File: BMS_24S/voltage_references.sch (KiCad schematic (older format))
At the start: 50 parts, among them Q201 BC558, U201 TL431LP, U202 LM324, U203 TL431LP, U204 TL431LP

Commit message: update balancing circuit
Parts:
- C202, C203, C205, C207, C209, C210: LCSC (none) -> C49678; Precision (none) -> 10%; Voltage (none) -> 50V
- R203, R204, R205, R207, R208, R209, R212, R213, R214, R215, R216, R217, R222, R223, R225, R228: LCSC (none) -> C17513; Power (none) -> 1/8W; Precision (none) -> 1%; Voltage (none) -> 150V
- R206, R220: LCSC (none) -> C17414; Power (none) -> 1/8W; Precision (none) -> 1%; Voltage (none) -> 150V

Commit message: updates made on BMS
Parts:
- renumbered C203 to C201, C204 to C202, C208 to C203, C209 to C204, C201 to C205, C202 to C206, C205 to C207, C206 to C208, C210 to C209, C211 to C210, C207 to C211, R225 to R202, R211 to R203, R213 to R204, R226 to R205, R215 to R206, R221 to R207, R223 to R208, R229 to R209, R202 to R210, R227 to R211, R208 to R212, R218 to R213, R228 to R215, R203 to R216, R205 to R217, R207 to R218, R209 to R219, R224 to R220, R212 to R221, R219 to R222, R230 to R223, R220 to R224, R222 to R225, R216 to R226, R210 to R227, R217 to R228, R204 to R229, R206 to R230, TP202 to TP201, TP203 to TP202, TP204 to TP203, TP201 to TP204, U202 to U201, U203 to U202, U201 to U203

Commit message: get BSPD
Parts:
- R201, R210: LCSC (none) -> C17408
- R203, R209, R213, R220, R222, R223, R227: LCSC (none) -> C17477
- U201: LCSC (none) -> C71035
- U202, U203, U204: LCSC (none) -> C181103
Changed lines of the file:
@@
 F 2 "Resistor_SMD:R_0805_2012Metric" V 930 950 50  0001 C CNN
 F 3 "~" H 1000 950 50  0001 C CNN
+F 4 "C17408" H 1000 950 50  0001 C CNN "LCSC"
 	1    1000 950
 	1    0    0    -1
@@
 F 2 "Package_SO:SOIC-14_3.9x8.7mm_P1.27mm" H 2300 1725 50  0001 C CNN
 F 3 "http://www.ti.com/lit/ds/symlink/lm2902-n.pdf" H 2350 2200 50  0001 C CNN
+F 4 "C71035" H 2300 2000 50  0001 C CNN "LCSC"
 	1    2300 2000
 	1    0    0    -1
@@
 F 2 "Package_SO:SOIC-14_3.9x8.7mm_P1.27mm" H 2300 725 50  0001 C CNN
 F 3 "http://www.ti.com/lit/ds/symlink/lm2902-n.pdf" H 2350 1200 50  0001 C CNN
+F 4 "C71035" H 2300 1000 50  0001 C CNN "LCSC"
 	2    2300 1000
 	1    0    0    -1
@@
 F 2 "Package_SO:SOIC-14_3.9x8.7mm_P1.27mm" H 5100 1675 50  0001 C CNN
 F 3 "http://www.ti.com/lit/ds/symlink/lm2902-n.pdf" H 5150 2150 50  0001 C CNN
+F 4 "C71035" H 5100 1950 50  0001 C CNN "LCSC"
 	3    5100 1950
 	1    0    0    -1
@@
 F 2 "Resistor_SMD:R_0805_2012Metric" V 930 1300 50  0001 C CNN
 F 3 "~" H 1000 1300 50  0001 C CNN
+F 4 "C17408" H 1000 1300 50  0001 C CNN "LCSC"
 	1    1000 1300
 	1    0    0    -1
@@
 F 2 "Package_TO_SOT_SMD:SOT-23" H 1000 1500 50  0001 C CIN
 F 3 "http://www.ti.com/lit/ds/symlink/tl431.pdf" H 1000 1650 50  0001 C CIN
+F 4 "C181103" H 1000 1650 50  0001 C CNN "LCSC"
 	1    1000 1650
 	0    1    -1   0
@@
 F 2 "Package_TO_SOT_SMD:SOT-23" H 3400 1100 50  0001 C CIN
 F 3 "http://www.ti.com/lit/ds/symlink/tl431.pdf" H 3400 1250 50  0001 C CIN
+F 4 "C181103" H 3400 1250 50  0001 C CNN "LCSC"
 	1    3400 1250
 	0    1    -1   0
@@
 F 2 "Package_TO_SOT_SMD:SOT-23" H 4100 2000 50  0001 C CIN
 F 3 "http://www.ti.com/lit/ds/symlink/tl431.pdf" H 4100 2150 50  0001 C CIN
+F 4 "C181103" H 4100 2150 50  0001 C CNN "LCSC"
 	1    4100 2150
 	0    1    -1   0
@@
 F 2 "Resistor_SMD:R_0805_2012Metric" V 6680 1200 50  0001 C CNN
 F 3 "~" H 6750 1200 50  0001 C CNN
+F 4 "C17477" H 6750 1200 50  0001 C CNN "LCSC"
 	1    6750 1200
 	-1   0    0    1
@@
 F 2 "Resistor_SMD:R_0805_2012Metric" V 6180 1650 50  0001 C CNN
 F 3 "~" H 6250 1650 50  0001 C CNN
+F 4 "C17477" H 6250 1650 50  0001 C CNN "LCSC"
 	1    6250 1650
 	1    0    0    -1
@@
 F 2 "Package_SO:SOIC-14_3.9x8.7mm_P1.27mm" H 2250 2925 50  0001 C CNN
 F 3 "http://www.ti.com/lit/ds/symlink/lm2902-n.pdf" H 2300 3400 50  0001 C CNN
+F 4 "C71035" H 2250 3200 50  0001 C CNN "LCSC"
 	5    2250 3200
 	0    1    1    0
@@
 F 2 "Resistor_SMD:R_0805_2012Metric" V 2780 1000 50  0001 C CNN
 F 3 "~" H 2850 1000 50  0001 C CNN
+F 4 "C17477" H 2850 1000 50  0001 C CNN "LCSC"
 	1    2850 1000
 	0    1    1    0
@@
 F 2 "Resistor_SMD:R_0805_2012Metric" V 5380 1800 50  0001 C CNN
 F 3 "~" H 5450 1800 50  0001 C CNN
+F 4 "C17477" H 5450 1800 50  0001 C CNN "LCSC"
 	1    5450 1800
 	-1   0    0    1
@@
 F 2 "Resistor_SMD:R_0805_2012Metric" V 7080 1800 50  0001 C CNN
 F 3 "~" H 7150 1800 50  0001 C CNN
+F 4 "C17477" H 7150 1800 50  0001 C CNN "LCSC"
 	1    7150 1800
 	-1   0    0    1
@@
 F 2 "Resistor_SMD:R_0805_2012Metric" V 2680 2200 50  0001 C CNN
 F 3 "~" H 2750 2200 50  0001 C CNN
+F 4 "C17477" H 2750 2200 50  0001 C CNN "LCSC"
 	1    2750 2200
 	1    0    0    -1
@@
 F 2 "Resistor_SMD:R_0805_2012Metric" V 5380 1400 50  0001 C CNN
 F 3 "~" H 5450 1400 50  0001 C CNN
+F 4 "C17477" H 5450 1400 50  0001 C CNN "LCSC"
 	1    5450 1400
 	-1   0    0    1
@@
 F 2 "Package_SO:SOIC-14_3.9x8.7mm_P1.27mm" H 6800 1775 50  0001 C CNN
 F 3 "http://www.ti.com/lit/ds/symlink/lm2902-n.pdf" H 6850 2250 50  0001 C CNN
+F 4 "C71035" H 6800 2050 50  0001 C CNN "LCSC"
 	4    6800 2050
 	1    0    0    -1

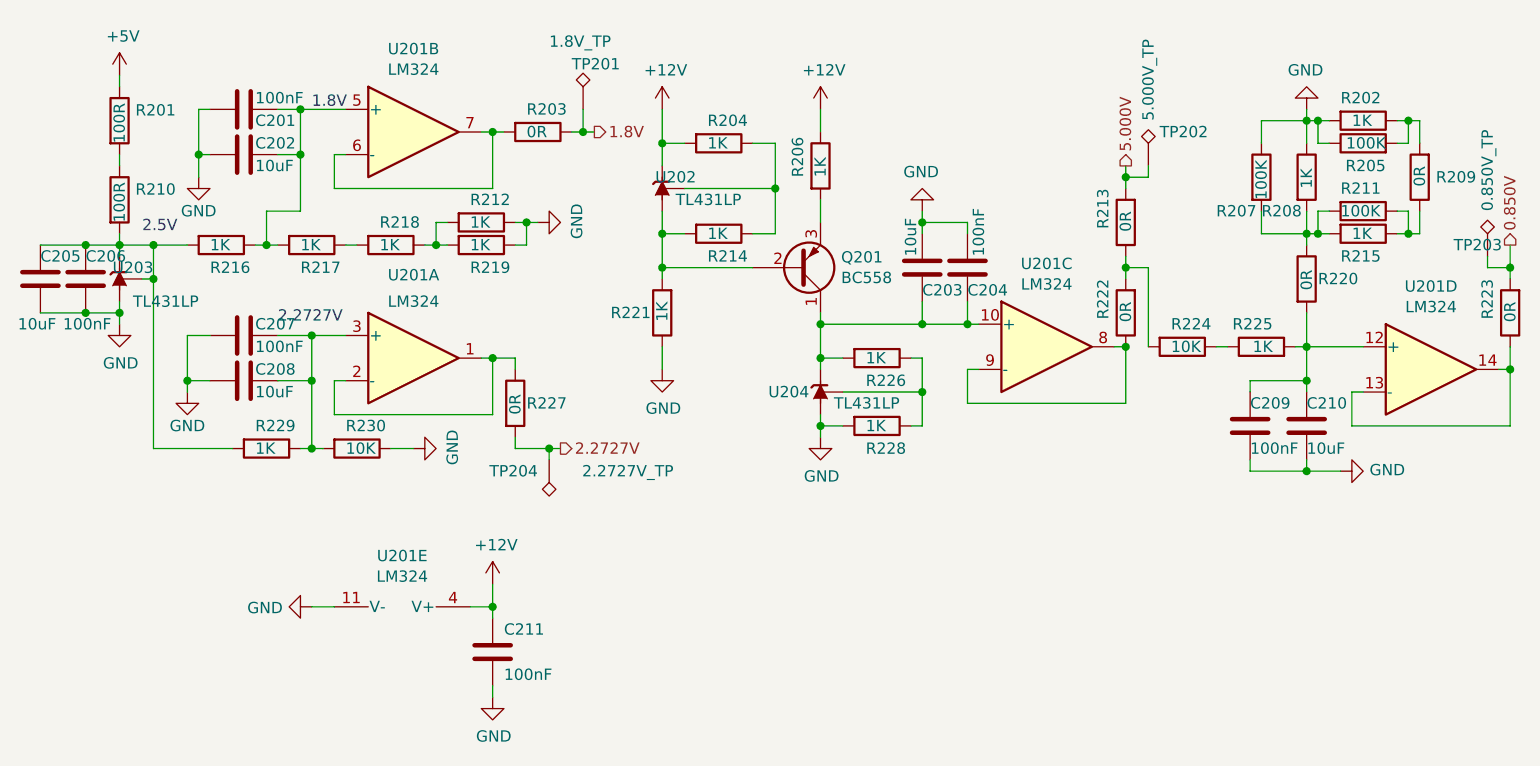
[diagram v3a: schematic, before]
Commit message: update bms pcb
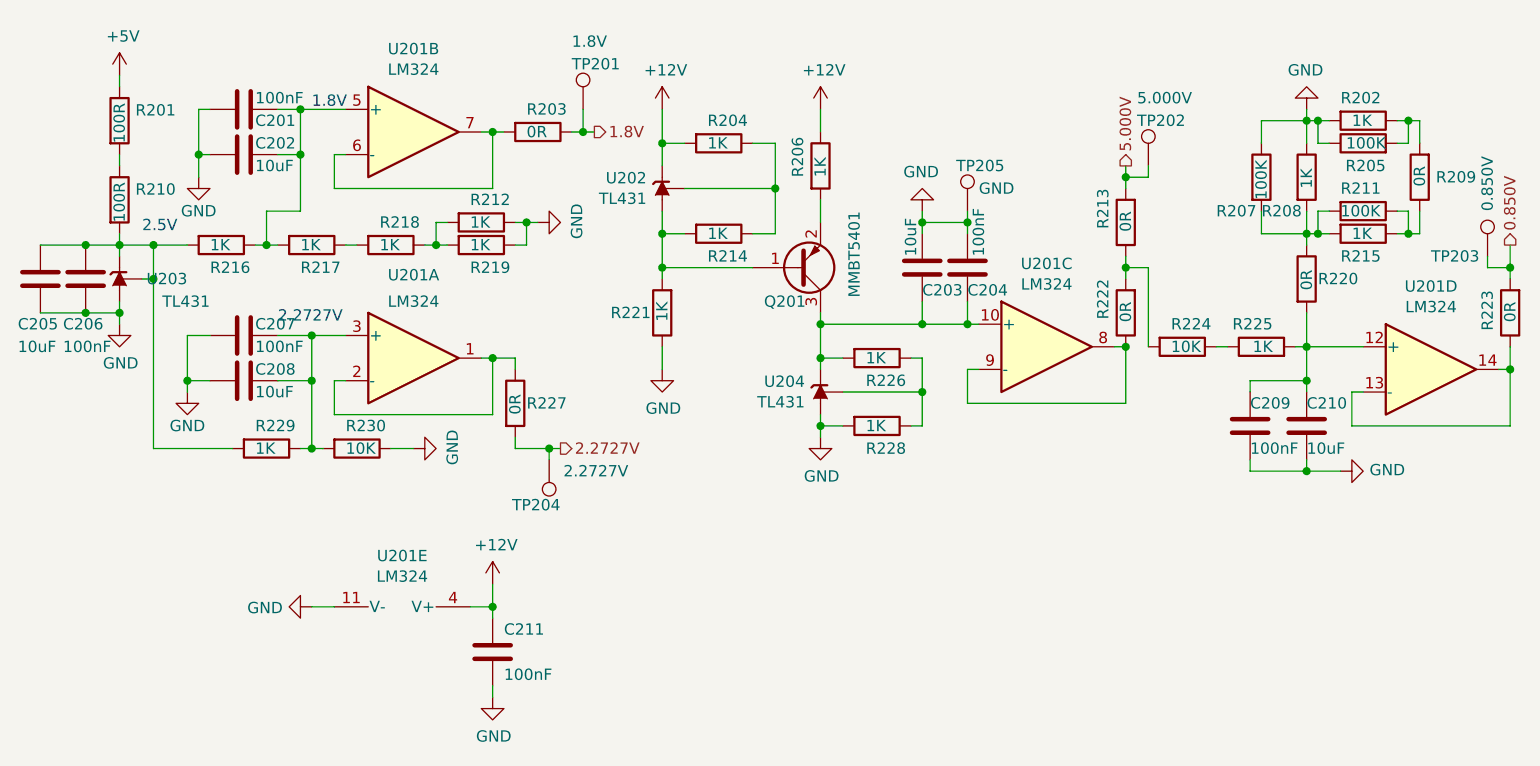
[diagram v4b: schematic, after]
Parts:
- removed Q201: BC558, Package_TO_SOT_SMD:SOT-23, symbol Transistor_BJT:BC558
- removed TP201: 1.8V_TP, TestPoint:TestPoint_Pad_2.5x2.5mm, symbol Connector:TestPoint_Alt
- removed TP202: 5.000V_TP, TestPoint:TestPoint_Pad_2.5x2.5mm, symbol Connector:TestPoint_Alt
- removed TP203: 0.850V_TP, TestPoint:TestPoint_Pad_2.5x2.5mm, symbol Connector:TestPoint_Alt
- removed TP204: 2.2727V_TP, TestPoint:TestPoint_Pad_2.5x2.5mm, symbol Connector:TestPoint_Alt
- removed U202, U203, U204: TL431LP, Package_TO_SOT_SMD:SOT-23, symbol e-Power:TL431LP
- added Q201: MMBT5401, Package_TO_SOT_SMD:SOT-23, symbol Transistor_BJT:MMBTA92
- added TP201: 1.8V, e-Power:TestPoint_Pad_D1.0mm, symbol Connector:TestPoint
- added TP202: 5.000V, e-Power:TestPoint_Pad_D1.0mm, symbol Connector:TestPoint
- added TP203: 0.850V, e-Power:TestPoint_Pad_D1.0mm, symbol Connector:TestPoint
- added TP204: 2.2727V, e-Power:TestPoint_Pad_D1.0mm, symbol Connector:TestPoint
- added TP205: GND, e-Power:TestPoint_Pad_D1.0mm, symbol Connector:TestPoint
- added U202, U204: TL431, Package_TO_SOT_SMD:SOT-23, symbol e-Power:TL431
- added U203: TL431, Package_TO_SOT_SMD:SOT-23, symbol Reference_Voltage:TL432DBZ
- C202, C203, C205, C208, C210: LCSC (none) -> C15850
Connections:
- net +12V: now also U202.2 (K)
- net 0.850V: now also TP203.1
- net 1.8V: now also TP201.1
- net 2.2727V: now also TP204.1
- net 5.000V: now also TP202.1
- net GND: now also TP205.1, U203.3 (A), U204.3 (A)
- net at C203.2, C204.2, R226.2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: now also Q201.3 (C), U204.2 (K)
- net at C205.1, C206.1, R210.2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: now also U203.1 (REF), U203.2 (K)
- net at R204.1, R214.1: now also U202.1 (REF)
- net at R214.2, R221.2: now also Q201.1 (B), U202.3 (A)
- net at R206.2: now also Q201.2 (E)
- net at R226.1, R228.1: now also U204.1 (REF)
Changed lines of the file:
@@
-$EndComp
-$Comp
-L e-Power:TL431LP U203
-U 1 1 5EB8B33D
-P 1000 1650
-F 0 "U203" V 1050 1800 50  0000 R CNN
-F 1 "TL431LP" V 900 2000 50  0000 R CNN
-F 2 "Package_TO_SOT_SMD:SOT-23" H 1000 1500 50  0001 C CIN
-F 3 "http://www.ti.com/lit/ds/symlink/tl431.pdf" H 1000 1650 50  0001 C CIN
-F 4 "C181103" H 1000 1650 50  0001 C CNN "LCSC"
-	1    1000 1650
-	0    1    -1   0
 $EndComp
 $Comp
@@
 U 1 1 5EB8E025
 P 850 1650
-F 0 "C206" H 850 1750 50  0000 L CNN
-F 1 "100nF" H 750 1450 50  0000 L CNN
+F 0 "C206" H 750 1450 50  0000 L CNN
+F 1 "100nF" H 750 1350 50  0000 L CNN
 F 2 "Capacitor_SMD:C_0805_2012Metric" H 888 1500 50  0001 C CNN
 F 3 "https://datasheet.lcsc.com/szlcsc/YAGEO-CC0805KRX7R9BB104_C49678.pdf" H 850 1650 50  0001 C CNN
@@
 U 1 1 5EB8ED80
 P 650 1650
-F 0 "C205" H 650 1750 50  0000 L CNN
-F 1 "10uF" H 550 1450 50  0000 L CNN
+F 0 "C205" H 550 1450 50  0000 L CNN
+F 1 "10uF" H 550 1350 50  0000 L CNN
 F 2 "Capacitor_SMD:C_0805_2012Metric" H 688 1500 50  0001 C CNN
 F 3 "~" H 650 1650 50  0001 C CNN
+F 4 "C15850" H 650 1650 50  0001 C CNN "LCSC"
 	1    650  1650
 	1    0    0    -1
@@
 F 2 "Capacitor_SMD:C_0805_2012Metric" H 1588 1950 50  0001 C CNN
 F 3 "~" H 1550 2100 50  0001 C CNN
+F 4 "C15850" H 1550 2100 50  0001 C CNN "LCSC"
 	1    1550 2100
 	0    1    1    0
@@
 F 2 "Capacitor_SMD:C_0805_2012Metric" H 1588 950 50  0001 C CNN
 F 3 "~" H 1550 1100 50  0001 C CNN
+F 4 "C15850" H 1550 1100 50  0001 C CNN "LCSC"
 	1    1550 1100
 	0    1    1    0
@@
 Wire Wire Line
 	2400 1500 2450 1500
-$Comp
-L e-Power:TL431LP U202
-U 1 1 5EBF269C
-P 3400 1250
-F 0 "U202" V 3450 1400 50  0000 R CNN
-F 1 "TL431LP" V 3350 1600 50  0000 R CNN
-F 2 "Package_TO_SOT_SMD:SOT-23" H 3400 1100 50  0001 C CIN
-F 3 "http://www.ti.com/lit/ds/symlink/tl431.pdf" H 3400 1250 50  0001 C CIN
-F 4 "C181103" H 3400 1250 50  0001 C CNN "LCSC"
-	1    3400 1250
-	0    1    -1   0
-$EndComp
 $Comp
 L power:+12V #PWR0202
@@
 	3400 1450 3400 1600
 $Comp
-L Transistor_BJT:BC558 Q201
-U 1 1 5EC10A29
-P 4000 1600
-F 0 "Q201" H 4191 1554 50  0000 L CNN
-F 1 "BC558" H 4191 1645 50  0000 L CNN
-F 2 "Package_TO_SOT_SMD:SOT-23" H 4200 1525 50  0001 L CIN
-F 3 "http://www.fairchildsemi.com/ds/BC/BC557.pdf" H 4000 1600 50  0001 L CNN
-	1    4000 1600
-	1    0    0    1
-$EndComp
-$Comp
 L Device:R R206
 U 1 1 5EC13E72
@@
 	3400 1600 3400 1650
 $Comp
-L e-Power:TL431LP U204
-U 1 1 5EC1FBC6
-P 4100 2150
-F 0 "U204" V 4100 2100 50  0000 R CNN
-F 1 "TL431LP" V 4050 2500 50  0000 R CNN
-F 2 "Package_TO_SOT_SMD:SOT-23" H 4100 2000 50  0001 C CIN
-F 3 "http://www.ti.com/lit/ds/symlink/tl431.pdf" H 4100 2150 50  0001 C CIN
-F 4 "C181103" H 4100 2150 50  0001 C CNN "LCSC"
-	1    4100 2150
-	0    1    -1   0
-$EndComp
-$Comp
 L power:GND #PWR0211
 U 1 1 5EC2095C
@@
 F 2 "Capacitor_SMD:C_0805_2012Metric" H 4588 1450 50  0001 C CNN
 F 3 "~" H 4550 1600 50  0001 C CNN
+F 4 "C15850" H 4550 1600 50  0001 C CNN "LCSC"
 	1    4550 1600
 	1    0    0    -1
@@
 F 2 "Capacitor_SMD:C_0805_2012Metric" H 6288 2150 50  0001 C CNN
 F 3 "~" H 6250 2300 50  0001 C CNN
+F 4 "C15850" H 6250 2300 50  0001 C CNN "LCSC"
 	1    6250 2300
 	1    0    0    -1
@@
 U 1 1 5EBB9479
 P 7150 1800
-F 0 "R223" V 7250 1650 50  0000 L CNN
+F 0 "R223" V 7250 1700 50  0000 L CNN
 F 1 "0R" V 7150 1750 50  0000 L CNN
 F 2 "Resistor_SMD:R_0805_2012Metric" V 7080 1800 50  0001 C CNN
@@
 	1    0    0    -1
 $EndComp
-$Comp
-L Connector:TestPoint_Alt TP?
-U 1 1 5EE4B789
-P 3050 900
-AR Path="/5ED9340F/5EE4B789" Ref="TP?"  Part="1"
-AR Path="/5EC1D7DE/5EE4B789" Ref="TP201"  Part="1"
-F 0 "TP201" H 3000 1100 50  0000 L CNN
-F 1 "1.8V_TP" H 2900 1200 50  0000 L CNN
-F 2 "TestPoint:TestPoint_Pad_2.5x2.5mm" H 3250 900 50  0001 C CNN
-F 3 "~" H 3250 900 50  0001 C CNN
-	1    3050 900
-	1    0    0    -1
-$EndComp
 Wire Wire Line
 	3050 900  3050 1000
@@
 Wire Wire Line
 	3050 1000 3000 1000
-$Comp
-L Connector:TestPoint_Alt TP?
-U 1 1 5EE5EAA4
+Wire Wire Line
+	2900 2450 2900 2400
+Connection ~ 2900 2400
+Wire Wire Line
+	2900 2400 2950 2400
+Wire Wire Line
+	5450 1150 5450 1200
+Wire Wire Line
+	5550 1150 5550 1200
+Wire Wire Line
+	5550 1200 5450 1200
+Connection ~ 5450 1200
+Wire Wire Line
+	5450 1200 5450 1250
+Wire Wire Line
+	7150 1500 7150 1600
+Wire Wire Line
+	7050 1550 7050 1600
+Wire Wire Line
+	7050 1600 7150 1600
+Connection ~ 7150 1600
+Wire Wire Line
+	7150 1600 7150 1650
+$Comp
+L Connector:TestPoint TP?
+U 1 1 5FB7FD92
 P 2900 2450
-AR Path="/5ED9340F/5EE5EAA4" Ref="TP?"  Part="1"
-AR Path="/5EC1D7DE/5EE5EAA4" Ref="TP204"  Part="1"
-F 0 "TP204" H 2950 2500 50  0000 L CNN
-F 1 "2.2727V_TP" H 2350 2500 50  0000 L CNN
-F 2 "TestPoint:TestPoint_Pad_2.5x2.5mm" H 3100 2450 50  0001 C CNN
+AR Path="/5ED9340F/5FB7FD92" Ref="TP?"  Part="1"
+AR Path="/5EC1D7DE/5FB7FD92" Ref="TP204"  Part="1"
+F 0 "TP204" H 2850 2650 50  0000 L CNN
+F 1 "2.2727V" H 2550 2500 50  0000 L CNN
+F 2 "e-Power:TestPoint_Pad_D1.0mm" H 3100 2450 50  0001 C CNN
 F 3 "~" H 3100 2450 50  0001 C CNN
 	1    2900 2450
 	-1   0    0    1
 $EndComp
-Wire Wire Line
-	2900 2450 2900 2400
-Connection ~ 2900 2400
-Wire Wire Line
-	2900 2400 2950 2400
-Wire Wire Line
-	5450 1150 5450 1200
-$Comp
-L Connector:TestPoint_Alt TP?
-U 1 1 5EE87F64
+$Comp
+L Connector:TestPoint TP?
+U 1 1 5FB877AE
+P 3050 900
+AR Path="/5ED9340F/5FB877AE" Ref="TP?"  Part="1"
+AR Path="/5EC1D7DE/5FB877AE" Ref="TP201"  Part="1"
+F 0 "TP201" H 3000 1100 50  0000 L CNN
+F 1 "1.8V" H 3000 1200 50  0000 L CNN
+F 2 "e-Power:TestPoint_Pad_D1.0mm" H 3250 900 50  0001 C CNN
+F 3 "~" H 3250 900 50  0001 C CNN
+	1    3050 900
+	1    0    0    -1
+$EndComp
+$Comp
+L Connector:TestPoint TP?
+U 1 1 5FB88B6A
 P 5550 1150
-AR Path="/5ED9340F/5EE87F64" Ref="TP?"  Part="1"
-AR Path="/5EC1D7DE/5EE87F64" Ref="TP202"  Part="1"
-F 0 "TP202" H 5600 1300 50  0000 L CNN
-F 1 "5.000V_TP" V 5550 1350 50  0000 L CNN
-F 2 "TestPoint:TestPoint_Pad_2.5x2.5mm" H 5750 1150 50  0001 C CNN
+AR Path="/5ED9340F/5FB88B6A" Ref="TP?"  Part="1"
+AR Path="/5EC1D7DE/5FB88B6A" Ref="TP202"  Part="1"
+F 0 "TP202" H 5500 1350 50  0000 L CNN
+F 1 "5.000V" H 5500 1450 50  0000 L CNN
+F 2 "e-Power:TestPoint_Pad_D1.0mm" H 5750 1150 50  0001 C CNN
 F 3 "~" H 5750 1150 50  0001 C CNN
 	1    5550 1150
 	1    0    0    -1
 $EndComp
-Wire Wire Line
-	5550 1150 5550 1200
-Wire Wire Line
-	5550 1200 5450 1200
-Connection ~ 5450 1200
-Wire Wire Line
-	5450 1200 5450 1250
-Wire Wire Line
-	7150 1500 7150 1600
-$Comp
-L Connector:TestPoint_Alt TP?
-U 1 1 5EEB48C9
+$Comp
+L Connector:TestPoint TP?
+U 1 1 5FB89627
 P 7050 1550
-AR Path="/5ED9340F/5EEB48C9" Ref="TP?"  Part="1"
-AR Path="/5EC1D7DE/5EEB48C9" Ref="TP203"  Part="1"
-F 0 "TP203" H 6900 1600 50  0000 L CNN
-F 1 "0.850V_TP" V 7050 1750 50  0000 L CNN
-F 2 "TestPoint:TestPoint_Pad_2.5x2.5mm" H 7250 1550 50  0001 C CNN
+AR Path="/5ED9340F/5FB89627" Ref="TP?"  Part="1"
+AR Path="/5EC1D7DE/5FB89627" Ref="TP203"  Part="1"
+F 0 "TP203" H 6800 1550 50  0000 L CNN
+F 1 "0.850V" V 7050 1750 50  0000 L CNN
+F 2 "e-Power:TestPoint_Pad_D1.0mm" H 7250 1550 50  0001 C CNN
 F 3 "~" H 7250 1550 50  0001 C CNN
 	1    7050 1550
 	1    0    0    -1
 $EndComp
-Wire Wire Line
-	7050 1550 7050 1600
-Wire Wire Line
-	7050 1600 7150 1600
-Connection ~ 7150 1600
-Wire Wire Line
-	7150 1600 7150 1650
+$Comp
+L Transistor_BJT:MMBTA92 Q201
+U 1 1 5FB8ADEC
+P 4000 1600
+F 0 "Q201" H 3850 1750 50  0000 L CNN
+F 1 "MMBT5401" V 4250 1350 50  0000 L CNN
+F 2 "Package_TO_SOT_SMD:SOT-23" H 4200 1525 50  0001 L CIN
+F 3 "https://datasheet.lcsc.com/szlcsc/Changjiang-Electronics-Tech-CJ-MMBT5401_C8326.pdf" H 4000 1600 50  0001 L CNN
+F 4 "C8326" H 4000 1600 50  0001 C CNN "LCSC"
+	1    4000 1600
+	1    0    0    1
+$EndComp
+$Comp
+L Reference_Voltage:TL432DBZ U203
+U 1 1 5FB99557
+P 1000 1650
+F 0 "U203" V 1000 1950 50  0000 R CNN
+F 1 "TL431" V 900 2050 50  0000 R CNN
+F 2 "Package_TO_SOT_SMD:SOT-23" H 1000 1500 50  0001 C CIN
+F 3 "http://www.ti.com/lit/ds/symlink/tl431.pdf" H 1000 1650 50  0001 C CIN
+	1    1000 1650
+	0    1    -1   0
+$EndComp
+$Comp
+L e-Power:TL431 U202
+U 1 1 5FBA715A
+P 3400 1250
+F 0 "U202" V 3446 1181 50  0000 R CNN
+F 1 "TL431" V 3355 1181 50  0000 R CNN
+F 2 "Package_TO_SOT_SMD:SOT-23" H 3400 1100 50  0001 C CIN
+F 3 "http://www.ti.com/lit/ds/symlink/tl431.pdf" H 3400 1250 50  0001 C CIN
+	1    3400 1250
+	0    1    -1   0
+$EndComp
+$Comp
+L e-Power:TL431 U204
+U 1 1 5FBA816C
+P 4100 2150
+F 0 "U204" V 4146 2081 50  0000 R CNN
+F 1 "TL431" V 4055 2081 50  0000 R CNN
+F 2 "Package_TO_SOT_SMD:SOT-23" H 4100 2000 50  0001 C CIN
+F 3 "http://www.ti.com/lit/ds/symlink/tl431.pdf" H 4100 2150 50  0001 C CIN
+	1    4100 2150
+	0    1    -1   0
+$EndComp
+$Comp
+L Connector:TestPoint TP?
+U 1 1 5FC6D345
+P 4750 1350
+AR Path="/5ED9340F/5FC6D345" Ref="TP?"  Part="1"
+AR Path="/5EC1D7DE/5FC6D345" Ref="TP205"  Part="1"
+F 0 "TP205" H 4700 1550 50  0000 L CNN
+F 1 "GND" H 4800 1450 50  0000 L CNN
+F 2 "e-Power:TestPoint_Pad_D1.0mm" H 4950 1350 50  0001 C CNN
+F 3 "~" H 4950 1350 50  0001 C CNN
+	1    4750 1350
+	1    0    0    -1
+$EndComp
+Wire Wire Line
+	4750 1350 4750 1400
+Connection ~ 4750 1400
 $EndSCHEMATC

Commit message: updates made on BMS
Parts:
- renumbered TP205 to TP203, TP203 to TP204, TP204 to TP205
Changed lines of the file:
@@
 P 2900 2450
 AR Path="/5ED9340F/5FB7FD92" Ref="TP?"  Part="1"
-AR Path="/5EC1D7DE/5FB7FD92" Ref="TP204"  Part="1"
-F 0 "TP204" H 2850 2650 50  0000 L CNN
+AR Path="/5EC1D7DE/5FB7FD92" Ref="TP205"  Part="1"
+F 0 "TP205" H 2850 2650 50  0000 L CNN
 F 1 "2.2727V" H 2550 2500 50  0000 L CNN
 F 2 "e-Power:TestPoint_Pad_D1.0mm" H 3100 2450 50  0001 C CNN
@@
 P 7050 1550
 AR Path="/5ED9340F/5FB89627" Ref="TP?"  Part="1"
-AR Path="/5EC1D7DE/5FB89627" Ref="TP203"  Part="1"
-F 0 "TP203" H 6800 1550 50  0000 L CNN
+AR Path="/5EC1D7DE/5FB89627" Ref="TP204"  Part="1"
+F 0 "TP204" H 6800 1550 50  0000 L CNN
 F 1 "0.850V" V 7050 1750 50  0000 L CNN
 F 2 "e-Power:TestPoint_Pad_D1.0mm" H 7250 1550 50  0001 C CNN
@@
 P 4750 1350
 AR Path="/5ED9340F/5FC6D345" Ref="TP?"  Part="1"
-AR Path="/5EC1D7DE/5FC6D345" Ref="TP205"  Part="1"
-F 0 "TP205" H 4700 1550 50  0000 L CNN
+AR Path="/5EC1D7DE/5FC6D345" Ref="TP203"  Part="1"
+F 0 "TP203" H 4700 1550 50  0000 L CNN
 F 1 "GND" H 4800 1450 50  0000 L CNN
 F 2 "e-Power:TestPoint_Pad_D1.0mm" H 4950 1350 50  0001 C CNN

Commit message: updates made on bms, almost done
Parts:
- R205, R207, R211: LCSC (none) -> C17407
- U202, U203, U204: LCSC (none) -> C3113
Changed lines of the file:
@@
 F 2 "Resistor_SMD:R_0805_2012Metric" V 6430 1350 50  0001 C CNN
 F 3 "~" H 6500 1350 50  0001 C CNN
+F 4 "C17407" H 6500 1350 50  0001 C CNN "LCSC"
 	1    6500 1350
 	0    1    1    0
@@
 F 2 "Resistor_SMD:R_0805_2012Metric" V 6430 1050 50  0001 C CNN
 F 3 "~" H 6500 1050 50  0001 C CNN
+F 4 "C17407" H 6500 1050 50  0001 C CNN "LCSC"
 	1    6500 1050
 	0    -1   -1   0
@@
 F 2 "Resistor_SMD:R_0805_2012Metric" V 5980 1200 50  0001 C CNN
 F 3 "~" H 6050 1200 50  0001 C CNN
+F 4 "C17407" H 6050 1200 50  0001 C CNN "LCSC"
 	1    6050 1200
 	1    0    0    -1
@@
 F 2 "Package_TO_SOT_SMD:SOT-23" H 1000 1500 50  0001 C CIN
 F 3 "http://www.ti.com/lit/ds/symlink/tl431.pdf" H 1000 1650 50  0001 C CIN
+F 4 "C3113" H 1000 1650 50  0001 C CNN "LCSC"
 	1    1000 1650
 	0    1    -1   0
@@
 F 2 "Package_TO_SOT_SMD:SOT-23" H 3400 1100 50  0001 C CIN
 F 3 "http://www.ti.com/lit/ds/symlink/tl431.pdf" H 3400 1250 50  0001 C CIN
+F 4 "C3113" H 3400 1250 50  0001 C CNN "LCSC"
 	1    3400 1250
 	0    1    -1   0
@@
 F 2 "Package_TO_SOT_SMD:SOT-23" H 4100 2000 50  0001 C CIN
 F 3 "http://www.ti.com/lit/ds/symlink/tl431.pdf" H 4100 2150 50  0001 C CIN
+F 4 "C3113" H 4100 2150 50  0001 C CNN "LCSC"
 	1    4100 2150
 	0    1    -1   0
